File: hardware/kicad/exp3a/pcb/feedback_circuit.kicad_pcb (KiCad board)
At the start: 2 copper layers, 116 x 50 mm, 10 parts, among them J1 ind + forsyning, J2 FB ud, U1 IL300, U3 MCP601, U4 MCP601

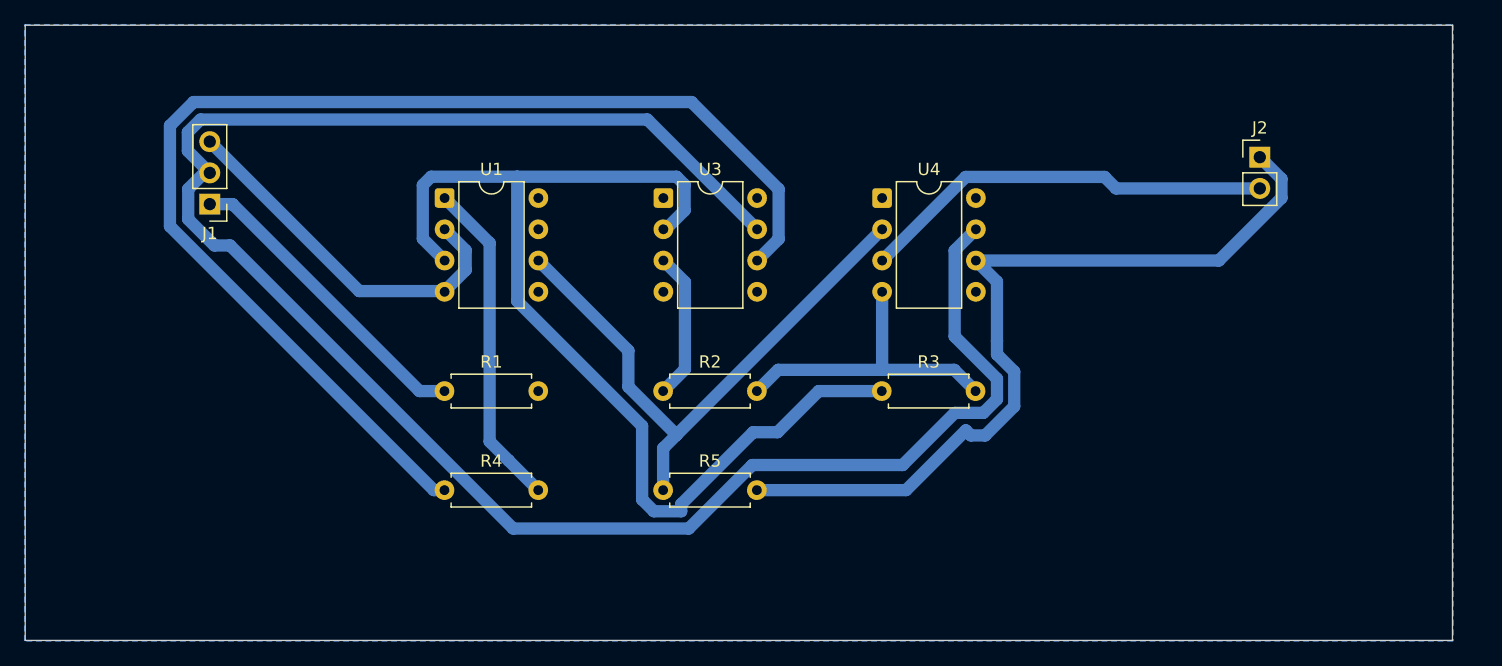
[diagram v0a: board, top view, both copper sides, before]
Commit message: Apply fiber-laser design rules from the DTU-PCB-prototyping guide
All seven boards rebuilt to meet the XTool fiber laser workflow
(SimsesLab/DTU-PCB-prototyping): 1.0 mm tracks, 0.8 mm clearance, solid
no-net fill zone on B.Cu (pad connection: none) so the laser only
engraves the isolation channels, DIP footprints switched to the
_LongPads variants from the guide's shop table.

TO packages cannot meet 0.8 mm pad-to-pad at stock sizes, so
energy_system.pretty now has TO-220-3_Vertical_LaserPads (pads narrowed
to 1.7 mm -> 0.84 mm gap; make_laserpads.py regenerates). The MPPT pass
transistor moves BD139 -> TIP41A (shop part): TO-126's 2.28 mm pitch can
never satisfy the rule, and TO-220 handles the ~7 W better anyway.

Two more bugs caught in this pass:
- Device:Q_NMOS uses letter pin numbers (G/D/S) while TO-220 pads are
  1/2/3 - buck/boost MOSFET pads silently got NO net in the earlier
  boards (no-net pads don't count as unconnected). pcb_build.py now maps
  G/D/S->1/2/3 and fails hard if a component ends up netless.
- DRC now 0 violations on all seven boards; remaining airwires are the
  documented jumpers.
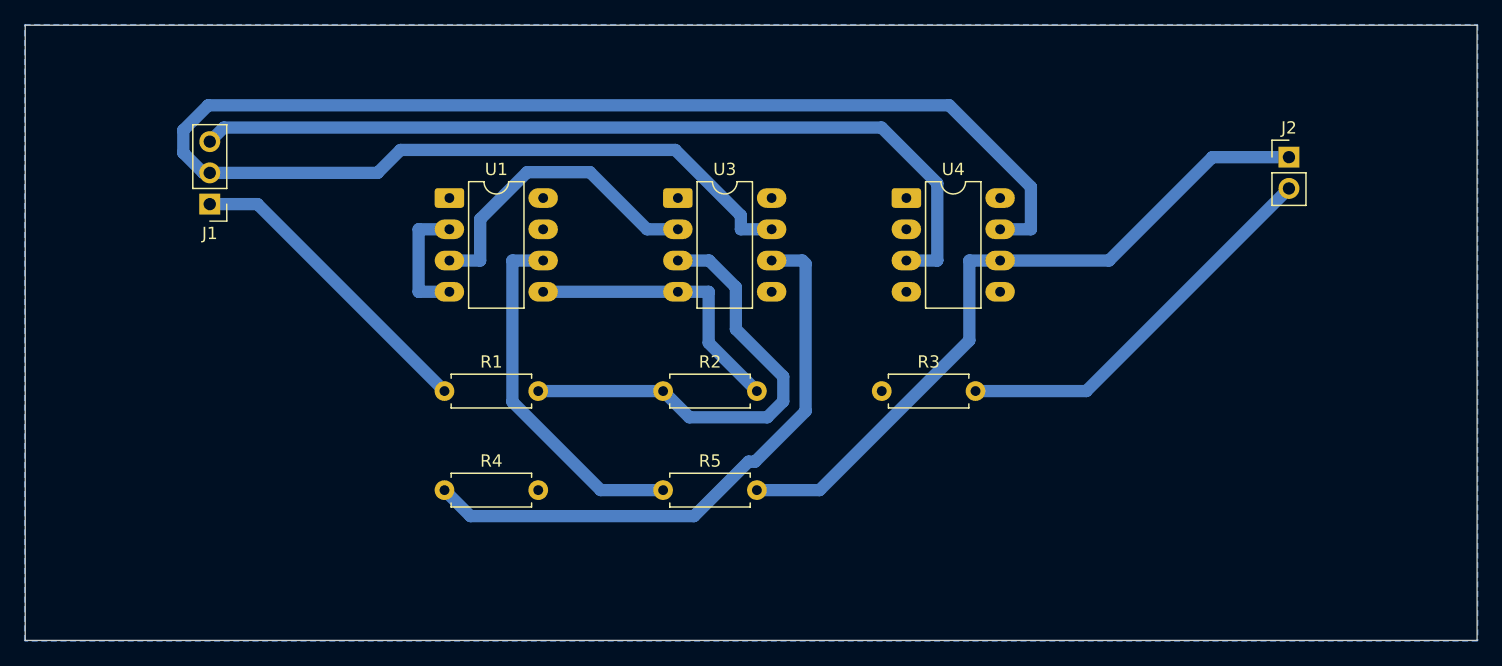
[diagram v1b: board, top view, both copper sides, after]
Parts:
- U1, U3, U4: footprint DIP-8_W7.62mm -> DIP-8_W7.62mm_LongPads
- moved J2 2.37 mm to (122.7, 30.7)
- moved U4 1.97 mm to (91.6, 34.0)
- moved U3 1.18 mm to (73.0, 34.0)
- moved U1 0.39 mm to (54.5, 34.0)
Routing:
- net /SERVO: track 87.8 -> 25.4 mm
- net /U3_OUT: track 99.1 -> 48.6 mm
- net GND: track 90.1 -> 135.8 mm
- net /LED: track 26.9 -> 0.00 mm
- net /IN_P: track 12.1 -> 37.8 mm
- net +5V: track 155.5 -> 132.8 mm
- net /OUT_PD: track 47.4 -> 29.2 mm
- net FB_OUT: track 68.2 -> 58.3 mm
- added copper zone on B.Cu, net (none)
- removed copper zone on B.Cu, net GND
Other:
- board size 116 x 50 mm -> 118 x 50 mm

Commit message: Engrave component references into the copper on all boards
The fiber laser has no silkscreen step, so the refdes (R1, U1, ...) are
placed as mirrored copper text on B.Cu next to each component - they
engrave in the same run as the traces and read correctly from the
solder side. Placement is collision-checked against tracks/pads/other
text (copper text over a track would short or sever it); tracks are
sampled into small boxes so diagonal runs don't false-positive. 86 of
96 labels fit; the handful dropped in dense spots are listed in
production/README.md and still appear on the F_Fab plots.

Also exports <board>_silk_top.dxf (F.Silkscreen + outline) per board as
an optional top-side engraving pass - run it on the component side
BEFORE the copper run, and do NOT mirror that one.

DRC still 0 violations on all seven; jumper lists updated.
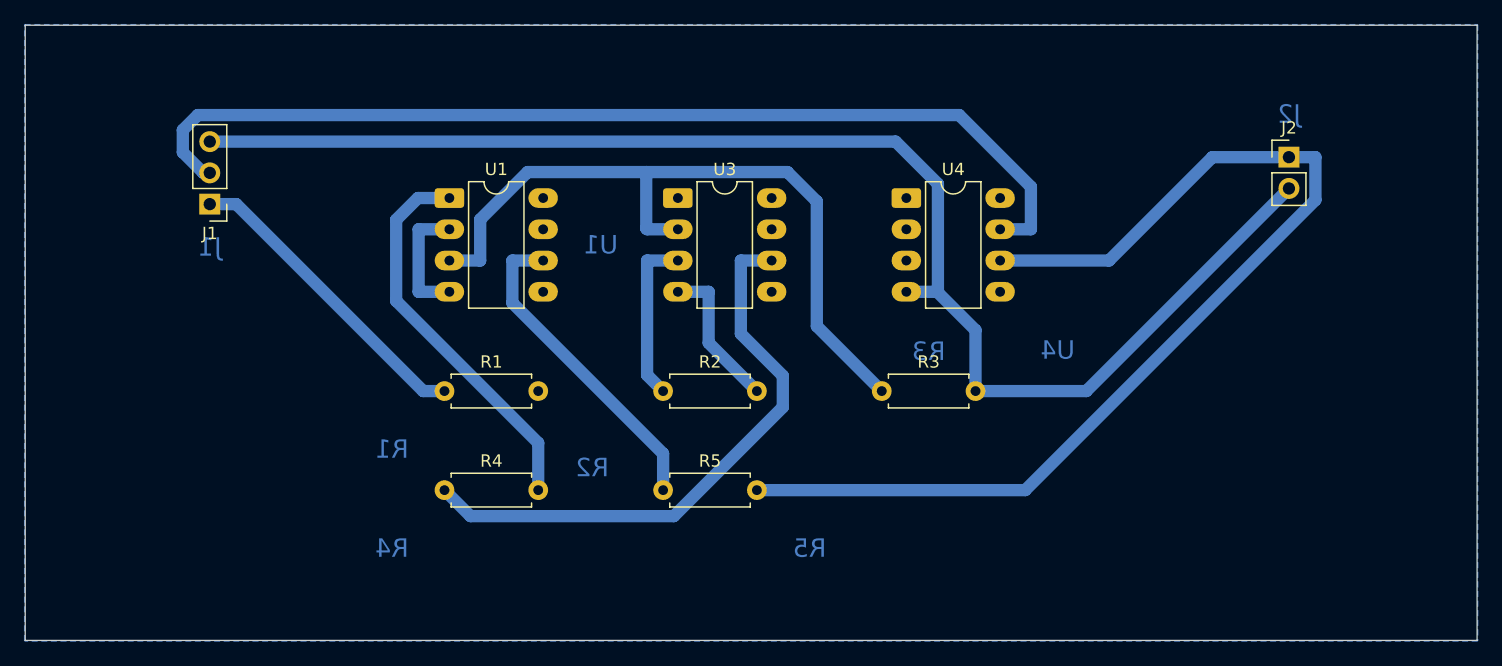
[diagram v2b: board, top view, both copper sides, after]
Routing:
- net +5V: track 132.8 -> 82.5 mm
- net /SERVO: track 25.4 -> 60.6 mm
- net /LED: track 0.00 -> 31.8 mm
- net FB_OUT: track 58.3 -> 87.7 mm
- net /IN_P: track 37.8 -> 13.7 mm
- net /OUT_PD: track 29.2 -> 26.2 mm
- net /U3_OUT: track 48.6 -> 47.9 mm
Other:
- board text added: "J1"
- board text added: "J2"
- board text added: "R1"
- board text added: "R2"
- board text added: "R3"
- board text added: "R4"
- board text added: "R5"
- board text added: "U1"
- board text added: "U4"
